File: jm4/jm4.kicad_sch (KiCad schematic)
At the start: 53 parts, among them J1 430450200, J2 430450200, J3 22035035, J4 22035035, U2 MC7812BDTRKG, U3 INA240A1PWR, U5 MCP2551-I_SN (CAN TRX), U7 TLV172IDCK, U8 ADS1118IRUGR

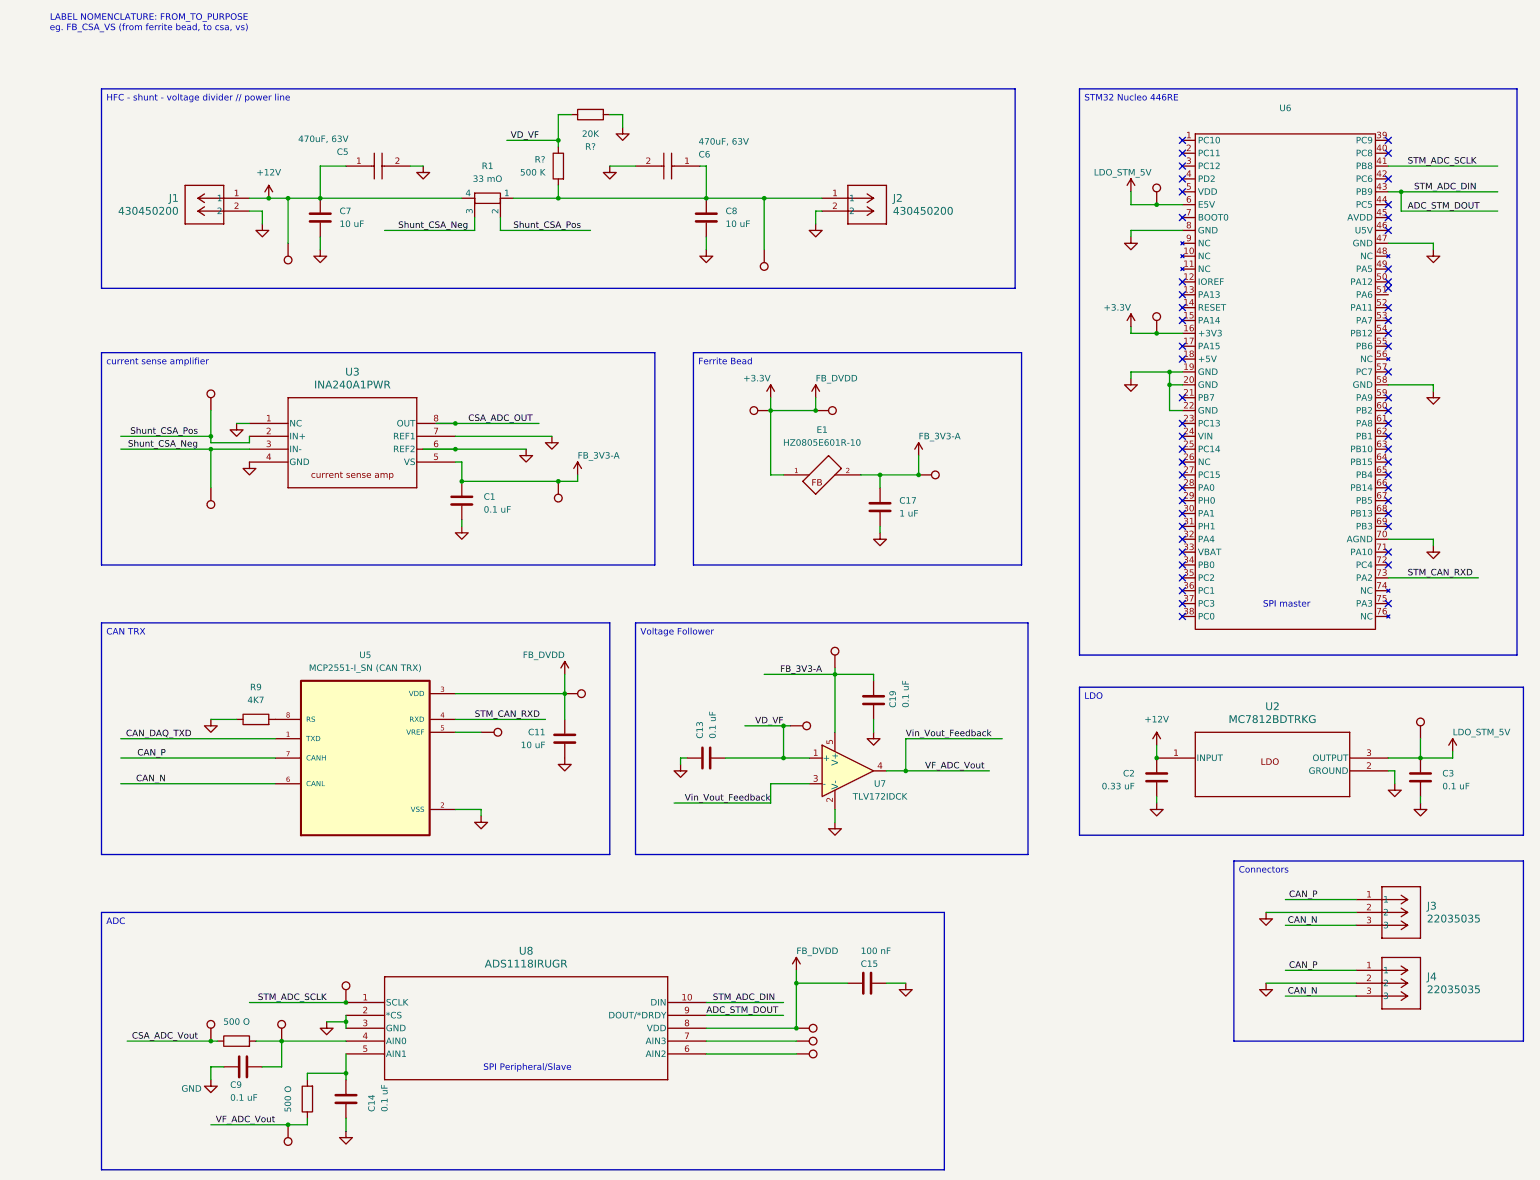
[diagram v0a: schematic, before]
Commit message: joulemeter layout - needs traces . also i hope this doesnt break anything teehee
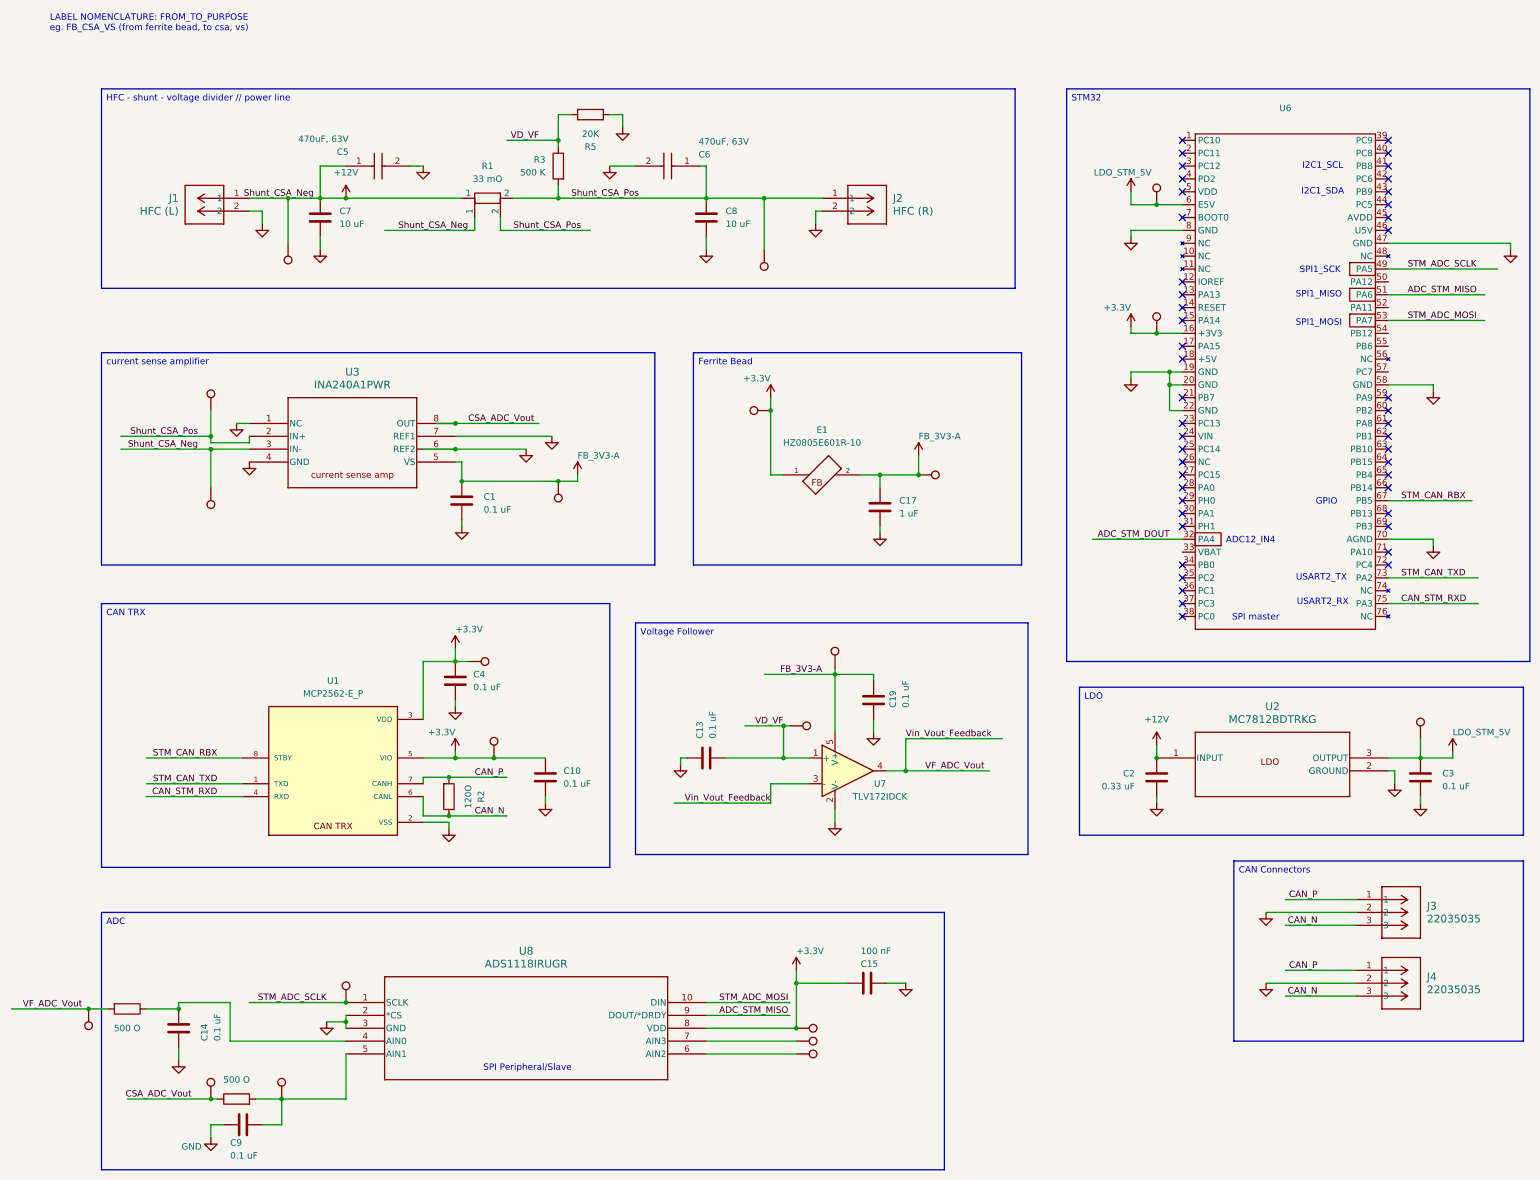
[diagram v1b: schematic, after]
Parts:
- removed C11: 10 uF, symbol Device:C
- removed R10: 500 O, symbol Device:R
- removed R9: 4K7, symbol Device:R
- removed TP6, TP? (x3): TestPoint, symbol Connector:TestPoint
- removed U5: MCP2551-I_SN (CAN TRX), MCP2551-I_SN:SOIC127P599X175-8N, symbol SMV_Custom:MCP2551-I_SN (CAN TRX)
- added C10, C4: 0.1 uF, Capacitor_SMD:C_0805_2012Metric_Pad1.18x1.45mm_HandSolder, symbol Device:C
- added R2: 120O, Resistor_SMD:R_0805_2012Metric_Pad1.20x1.40mm_HandSolder, symbol Device:R
- added R6: 500 O, Resistor_SMD:R_0805_2012Metric_Pad1.20x1.40mm_HandSolder, symbol Device:R
- added TP10, TP12, TP13: TestPoint, TestPoint:TestPoint_Pad_1.0x1.0mm, symbol Connector:TestPoint
- added U1: MCP2562-E_P, SMV_ICs:SOIC127P600X175-8N, symbol SMV_Custom:MCP2562-E_P
- C1, C13, C14, C15, C17, C19, C2, C3, C7, C8, C9: footprint (none) -> Capacitor_SMD:C_0805_2012Metric_Pad1.18x1.45mm_HandSolder
- E1: footprint HZ0805E601R-10:FB_HZ0805E601R-10 -> SMV_Passives:FB_HZ0805E601R-10
- J1: value 430450200 -> HFC (L)
- J2: value 430450200 -> HFC (R)
- R1: footprint (none) -> SMV_Passives:RES_PU3921_.5mOHM_YAG
- R3, R5: renamed from R?; footprint (none) -> Resistor_SMD:R_0805_2012Metric_Pad1.20x1.40mm_HandSolder
- R4: footprint (none) -> Resistor_SMD:R_0805_2012Metric_Pad1.20x1.40mm_HandSolder
- TP1, TP2, TP3, TP4, TP5, TP7, TP8: footprint (none) -> TestPoint:TestPoint_Pad_1.0x1.0mm
- TP11, TP14, TP15, TP16, TP17, TP19, TP20, TP21, TP22, TP6, TP9: renamed from TP?; footprint (none) -> TestPoint:TestPoint_Pad_1.0x1.0mm
- U2: footprint DPAK-3_ONS -> SMV_ICs:DPAK-3_ONS
- U3: footprint PW0008A_N_TEX -> SMV_ICs:PW0008A_N_TEX
- U8: footprint RUG10 -> SMV_ICs:RUG10 (ADS1118)
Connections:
- net CSA_ADC_OUT is gone; now on net CSA_ADC_Vout: U3.8 (OUT)
- net +12V: now also R1.1, TP5.1, U3.3 (IN-); no longer R1.4
- net +3.3V: now also C10.1, C4.1, TP12.1, TP13.1, U1.3 (VDD), U1.5 (VIO)
- net ADC_STM_DOUT: now also U6.32 (PA4); no longer U6.43 (PB9), U8.10 (DIN), U8.9 (DOUT/*DRDY)
- net CAN_N: now also R2.1, U1.6 (CANL)
- net CAN_P: now also R2.2, U1.7 (CANH)
- net GND: now also C10.2, C4.2, U1.2 (VSS)
- net STM_ADC_SCLK: now also U6.49 (PA5); no longer U6.41 (PB8)
- net Shunt_CSA_Pos: now also C6.1, C8.1, J2.1, R3.2, TP8.1
- net VF_ADC_Vout: now also R6.2, TP10.1
- net at C9.1, R4.2, TP9.1: now also U8.5 (AIN1); no longer U8.4 (AIN0)
- net at C14.1: now also U8.4 (AIN0), R6.1; no longer U8.5 (AIN1)
- net ADC_STM_MISO: now reaches U6.51 (PA6)
- net ADC_STM_MISO: now also U8.9 (DOUT/*DRDY)
- net STM_ADC_MOSI: now reaches U6.53 (PA7)
- net STM_ADC_MOSI: now also U8.10 (DIN)
- net STM_CAN_RBX: now reaches U6.67 (PB5)
- net STM_CAN_RBX: now also U1.8 (STBY)
- net CAN_STM_RXD: now reaches U6.75 (PA3)
- net CAN_STM_RXD: now also U1.4 (RXD)
- net STM_CAN_RXD renamed STM_CAN_TXD
- net STM_CAN_TXD: now also U1.1 (TXD)
- removed net Shunt_CSA_Neg: R1.3, TP5.1, U3.3 (IN-)
- no-connect marks 57 -> 47
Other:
- note added: "ADC12_IN4"
- note added: "GPIO"
- note added: "I2C1_SCL"
- note added: "I2C1_SDA"
- note added: "SPI1_MISO"
- note added: "SPI1_MOSI"
- note added: "SPI1_SCK"
- note added: "USART2_RX"
- note added: "USART2_TX"
- moved on the sheet: C14, C9, R1
